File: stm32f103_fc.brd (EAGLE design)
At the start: 53.1 x 76.5 mm, 50 parts, among them IC1 STM32F103C8T6, IC2 LD1117AS33TR, Y1 8MHz, Y2 32.768MHz

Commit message: fix
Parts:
- flipped C22 to the top
- flipped R10 to the top, turned to 180 degrees
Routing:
- net GND: track 239.0 -> 236.5 mm
- net PA12: track 56.3 -> 58.3 mm
- net PA11: track 5.78 -> 4.51 mm, vias 1 -> 0
- net VCC3V3: track 252.3 -> 251.2 mm
- net N$16: track 5.27 -> 5.71 mm, vias 1 -> 2
- net N$6: track 66.7 -> 67.0 mm, vias 5 -> 6

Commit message: version 1.0.1 done fix transistor
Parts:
- removed N-CHANNEL-MOSFET: 2N7002KT1G, adafruit:SOT23
- removed R12: 1omh, SparkFun-Resistors:0603
- added MOSFET-1: 2N7002KT1G, adafruit:SOT23
- added R14: 470omh, SparkFun-Resistors:0603
- R4: value 470omh -> 1omh
- moved R4 40.3 mm to (58.2, 30.6)
- moved R15 25.6 mm to (58.8, 43.0), turned to 270 degrees
- moved R5 16.8 mm to (55.2, 70.4), turned to 180 degrees
- moved SERVO_X 1.02 mm to (68.3, 47.0)
- moved PY1 0.76 mm to (63.6, 28.7)
- renumbered N-CHANNEL-MOSFET-2 to MOSFET-2
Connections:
- removed net N$15: N-CHANNEL-MOSFET.3, R12.1
- new net N$11: PY1.2, R4.2
- net GND: now also MOSFET-1.3, MOSFET-2.3, R14.2, R5.2; no longer MOSFET-2.2, N-CHANNEL-MOSFET.2, R4.1, R5.1
- net N$13: now also MOSFET-2.2; no longer MOSFET-2.3
- net N$14: now also MOSFET-1.2, R4.1; no longer PY1.2, R12.2
- net PB6: now also R14.1; no longer R5.2
- net PB7: now also MOSFET-1.1, R5.1; no longer N-CHANNEL-MOSFET.1, R4.2
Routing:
- net N$12: track 39.7 -> 7.45 mm, vias 2 -> 1
- net GND: track 236.5 -> 207.1 mm, vias 12 -> 10
- net N$13: track 7.87 -> 28.6 mm, vias 0 -> 2
- net N$15: track 10.5 -> 0.00 mm, vias 2 -> 0
- net N$11: track 0.00 -> 5.70 mm
- net N$14: track 51.5 -> 55.7 mm
- net N$17: track 28.8 -> 30.7 mm
- net PB7: track 42.1 -> 43.8 mm
- net PB6: track 29.2 -> 30.7 mm
- net 9V: track 165.4 -> 166.2 mm
- net PA6: track 22.2 -> 22.8 mm

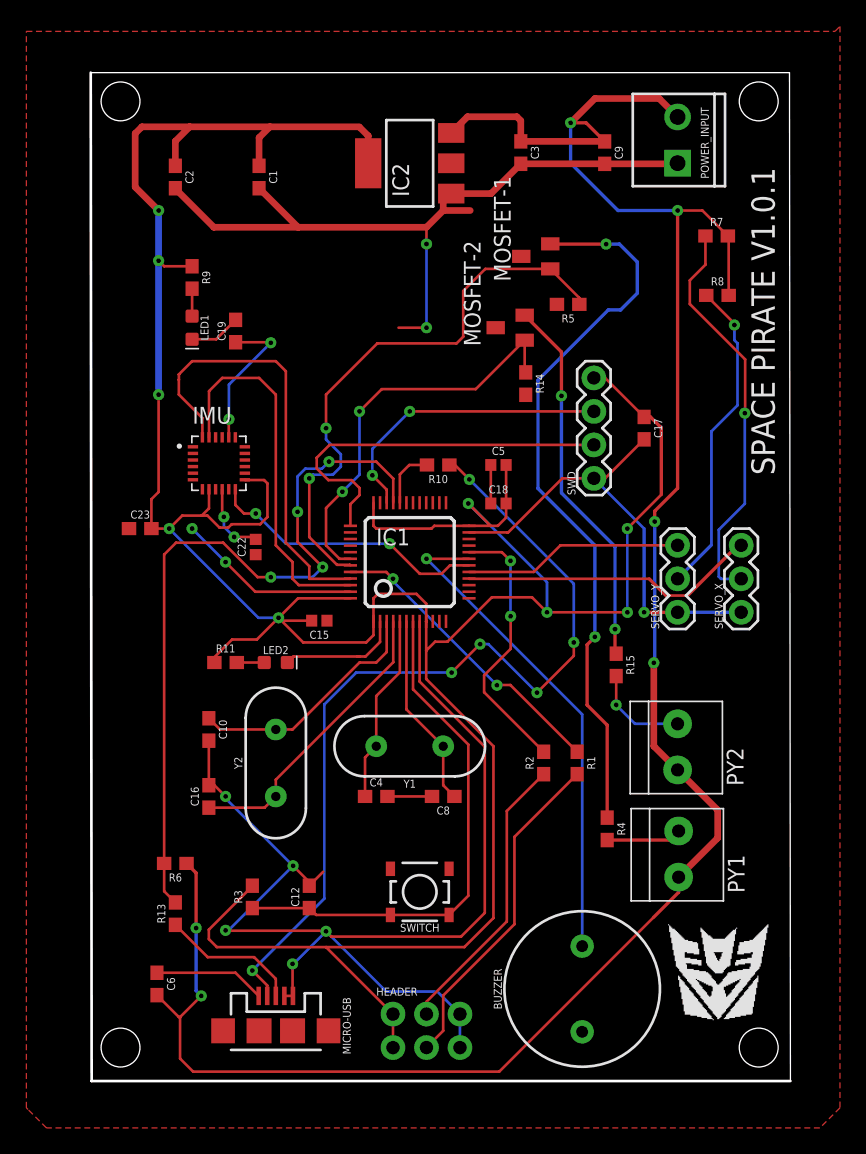
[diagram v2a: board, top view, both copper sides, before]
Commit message: four layer board done
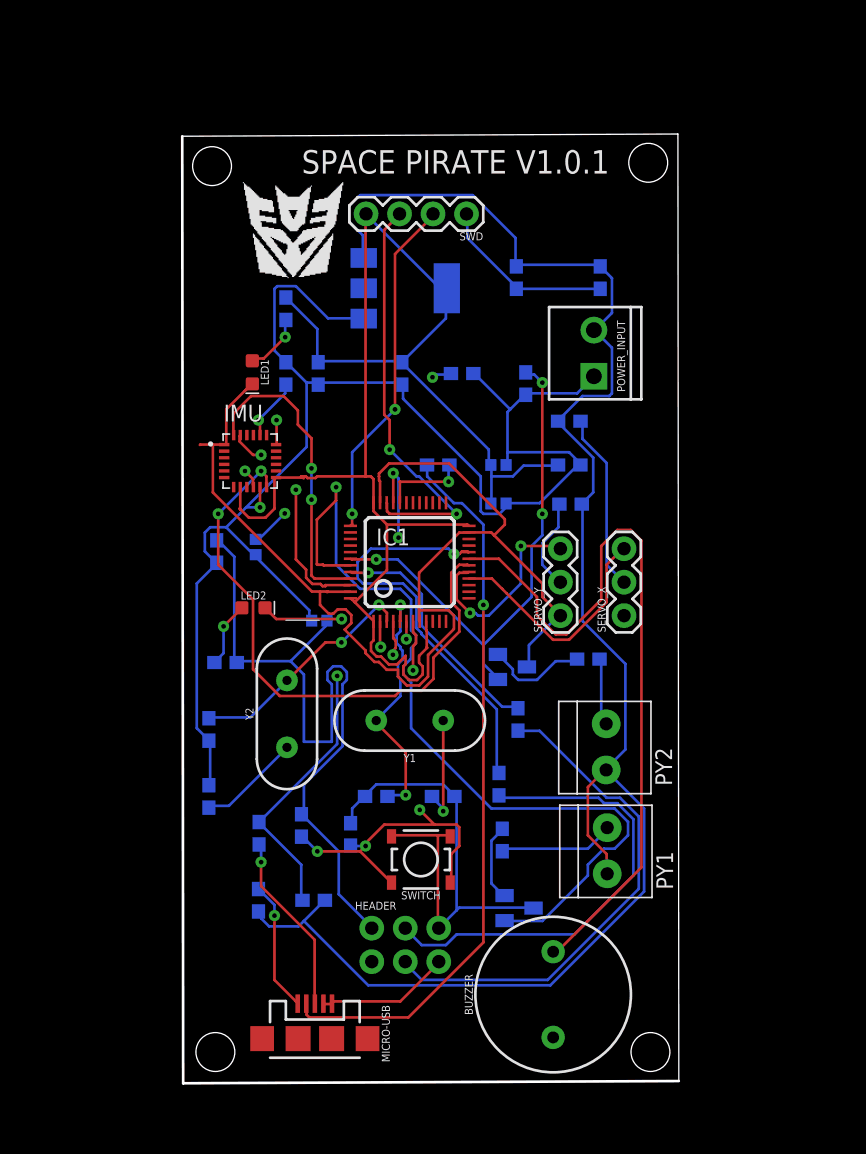
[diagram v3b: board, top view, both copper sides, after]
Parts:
- moved MOSFET-1 49.5 mm to (51.5, 24.6), flipped to the bottom
- moved MOSFET-2 25.7 mm to (51.0, 42.8), flipped to the bottom
- moved SWD 22.3 mm to (47.5, 77.2), turned to 180 degrees
- moved R8 19.4 mm to (55.4, 55.2), flipped to the bottom, turned to 180 degrees
- moved C1 18.4 mm to (42.6, 65.1), flipped to the bottom
- moved C2 18.4 mm to (36.2, 65.1), flipped to the bottom
- moved R7 18.0 mm to (55.3, 61.5), flipped to the bottom
- moved POWER_INPUT 17.4 mm to (57.2, 64.9)
- moved R6 10.9 mm to (35.9, 25.1), flipped to the bottom, turned to 0 degrees
- moved C6 9.98 mm to (31.7, 25.1), flipped to the bottom
- moved R5 9.60 mm to (47.2, 65.1), flipped to the bottom
- moved C3 9.49 mm to (51.3, 72.4), flipped to the bottom
- moved C9 9.49 mm to (57.6, 72.4), flipped to the bottom
- moved IC2 9.49 mm to (42.8, 71.6), flipped to the bottom
- moved SERVO_X 8.89 mm to (59.4, 46.7)
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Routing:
- net GND: track 207.1 -> 287.9 mm, vias 10 -> 2
- net VCC3V3: track 251.2 -> 172.4 mm, vias 9 -> 0
- net N$14: track 55.7 -> 5.84 mm, vias 2 -> 0
- net 9V: track 166.2 -> 130.1 mm, vias 6 -> 0
- net PB7: track 43.8 -> 78.1 mm
- net PB0: track 21.3 -> 44.6 mm
- net N$13: track 28.6 -> 7.69 mm, vias 2 -> 0
- net PB1: track 37.5 -> 56.5 mm, vias 1 -> 0
- net PA12: track 58.3 -> 40.6 mm, vias 4 -> 3
- net N$18: track 24.4 -> 7.03 mm, vias 1 -> 0
- net N$17: track 30.7 -> 13.6 mm, vias 1 -> 0
- net N$2: track 21.9 -> 35.3 mm
- net N$1: track 25.5 -> 38.6 mm
- net N$6: track 67.0 -> 55.0 mm, vias 6 -> 1
- net PB9: track 28.6 -> 17.0 mm, vias 0 -> 2
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- added copper zone on layer 15, net GND
- added copper zone on layer 2, net VCC3V3
- removed copper zone on layer 1, net GND
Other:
- board size 53.1 x 76.5 mm -> 37.7 x 72 mm

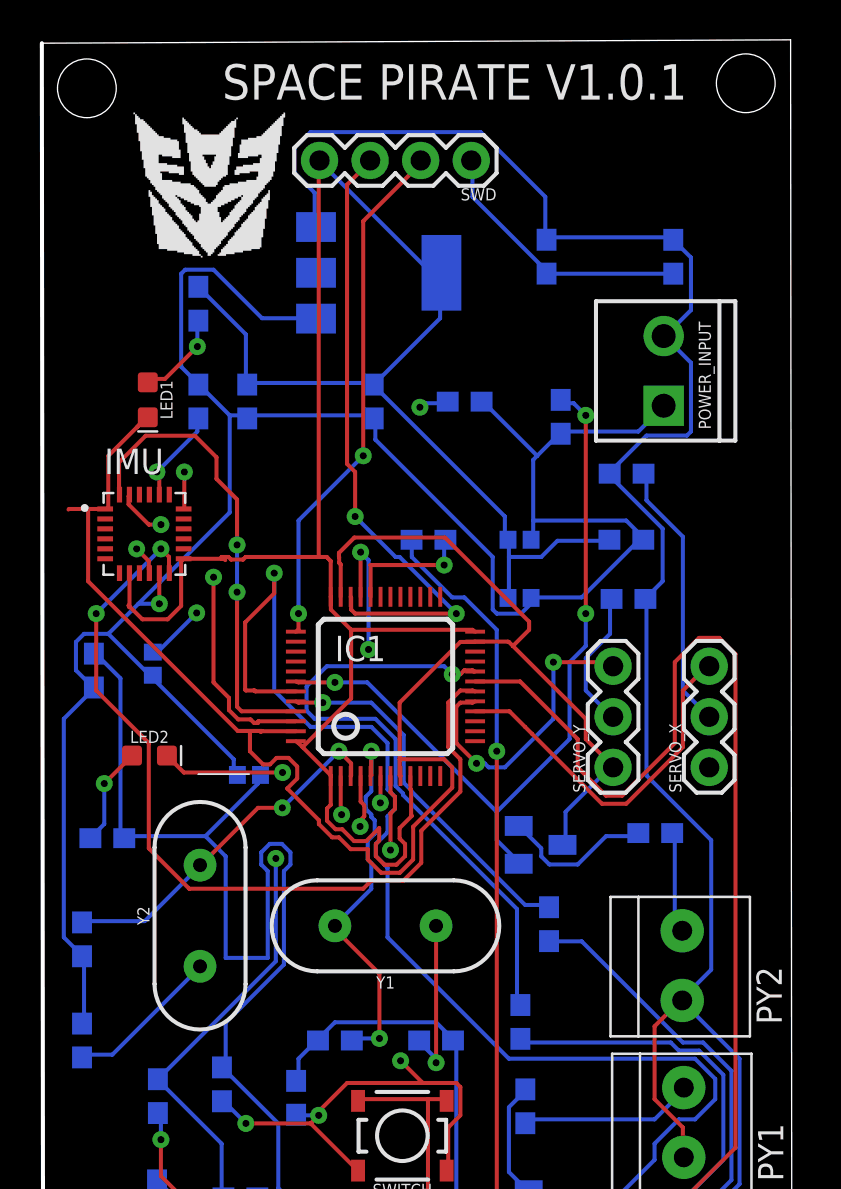
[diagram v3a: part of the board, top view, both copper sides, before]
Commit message: fixed mirror issue
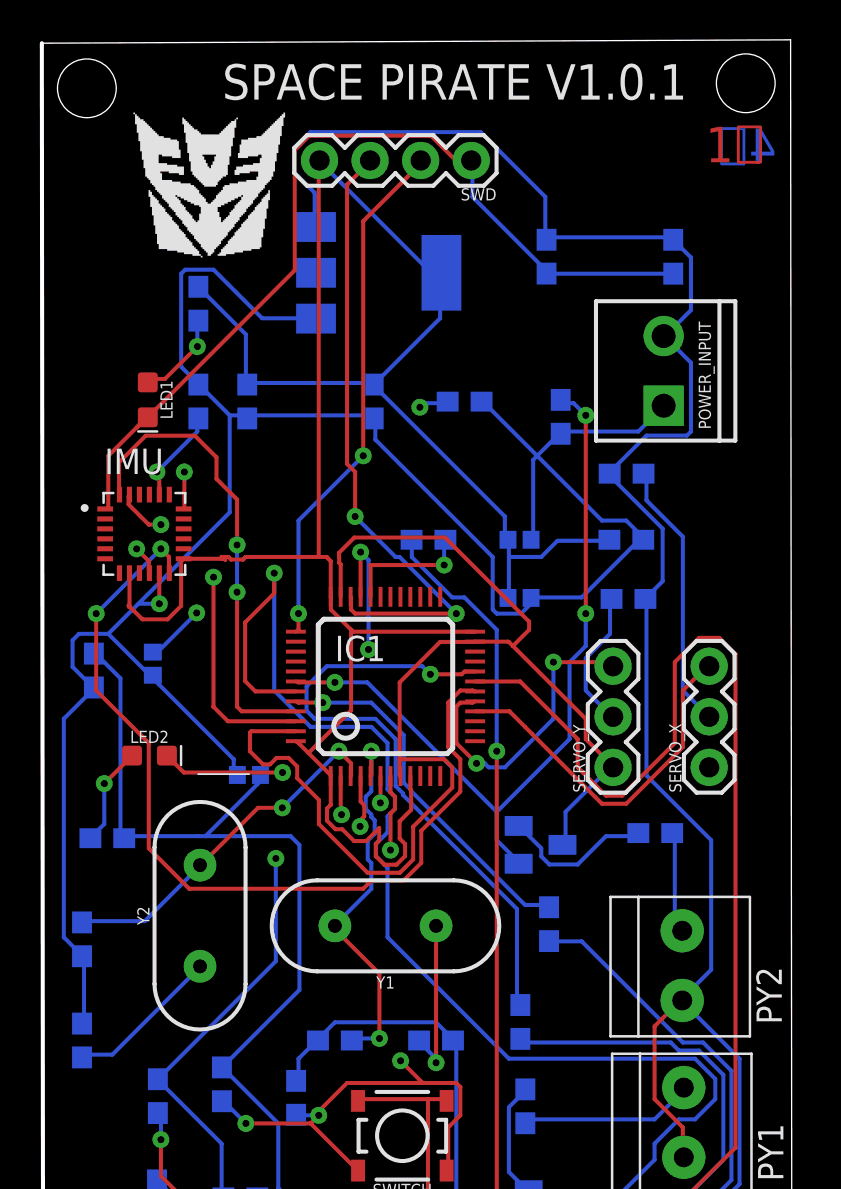
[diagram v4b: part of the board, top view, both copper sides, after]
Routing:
- net GND: track 287.9 -> 298.4 mm
- net VCC3V3: track 172.4 -> 162.2 mm
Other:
- board text added: "1层"
- board text added: "2层"
- board text added: "3层"
- board text added: "4层"

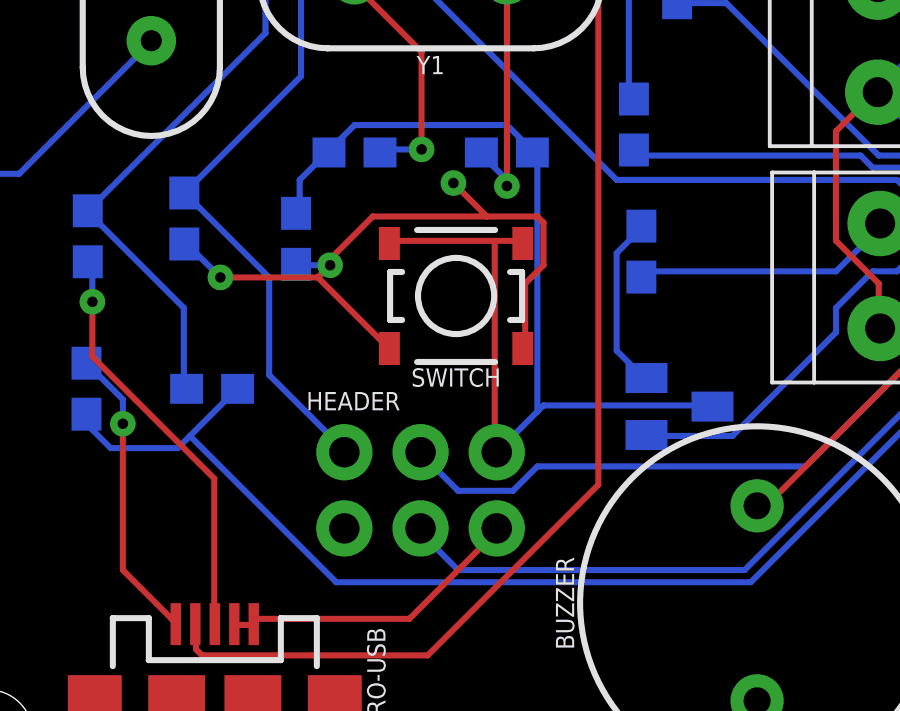
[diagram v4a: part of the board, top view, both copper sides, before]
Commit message: added new switch
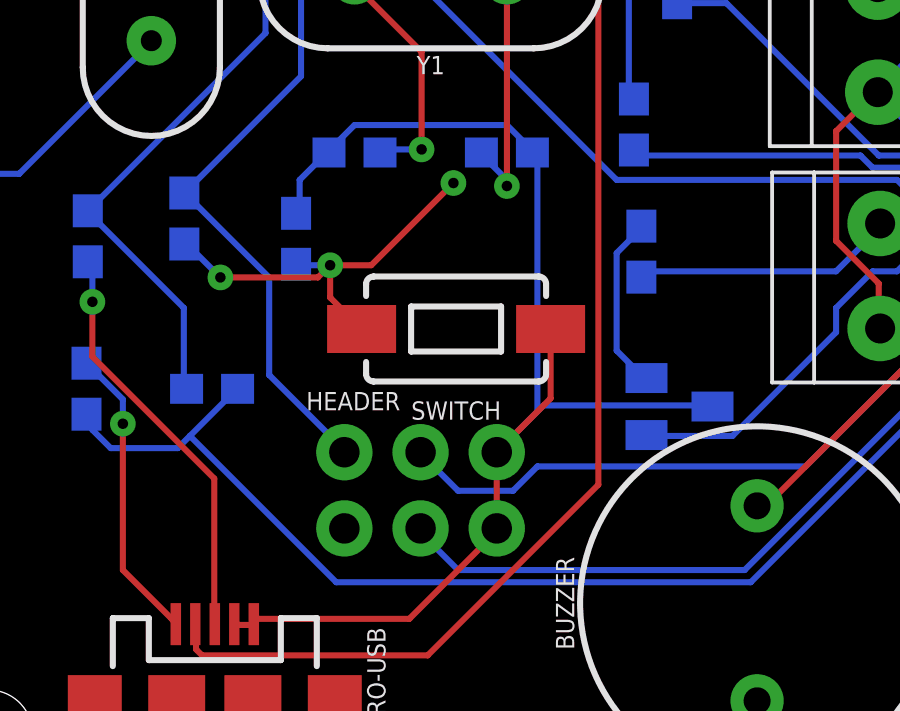
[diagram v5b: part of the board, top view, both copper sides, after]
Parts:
- SWITCH: device SparkFun-Switches:TACTILE_SWITCH_SMD_4.5MM -> SparkFun-Switches:TACTILE_SWITCH_SMD_6.0X3.5MM
- moved SWITCH 1.10 mm to (44.0, 27.1)
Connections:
- net GND: now also SWITCH.1; no longer SWITCH.2, SWITCH.3
- net RESET: now also SWITCH.2; no longer SWITCH.1, SWITCH.4
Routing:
- net RESET: track 38.7 -> 29.1 mm
- net GND: track 298.4 -> 294.2 mm
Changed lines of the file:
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@@
 <?xml version="1.0" encoding="utf-8"?>
 <!DOCTYPE eagle SYSTEM "eagle.dtd">
-<eagle version="9.3.1">
+<eagle version="9.3.0">
 <drawing>
 <settings>
@@
 <attribute name="VALUE" x="49.911" y="54.483" size="0.6096" layer="28" font="vector" ratio="20" rot="MR0" align="top-center"/>
 </element>
-<element name="SWITCH" library="SparkFun-Switches" library_urn="urn:adsk.eagle:library:535" package="TACTILE_SWITCH_SMD_4.5MM" package3d_urn="urn:adsk.eagle:package:40162/1" value="MOMENTARY-SWITCH-SPST-SMD-4.5MM-轻触开关" x="44.026659375" y="28.2360875" smashed="yes" rot="R180">
-<attribute name="NAME" x="44.026659375" y="25.8230875" size="0.6096" layer="21" font="vector" ratio="20" rot="R180" align="bottom-center"/>
-<attribute name="PROD_ID" value="SWCH-09213" x="44.026659375" y="28.2360875" size="1.778" layer="27" rot="R180" display="off"/>
-<attribute name="VALUE" x="44.026659375" y="30.6490875" size="0.6096" layer="27" font="vector" ratio="20" rot="R180" align="top-center"/>
+<element name="SWITCH" library="SparkFun-Switches" library_urn="urn:adsk.eagle:library:535" package="TACTILE_SWITCH_SMD_6.0X3.5MM" package3d_urn="urn:adsk.eagle:package:40165/1" value="MOMENTARY-SWITCH-SPST-SMD-4.5MM-轻触开关" x="44.0266625" y="27.13553125" smashed="yes" rot="R180">
+<attribute name="NAME" x="44.0266625" y="24.72253125" size="0.6096" layer="21" font="vector" ratio="20" rot="R180" align="bottom-center"/>
+<attribute name="PROD_ID" value="SWCH-00815" x="44.0266625" y="27.13553125" size="1.778" layer="27" rot="R180" display="off"/>
+<attribute name="SF_SKU" value="COM-08229" x="44.0266625" y="27.13553125" size="1.778" layer="27" rot="R180" display="off"/>
+<attribute name="VALUE" x="44.0266625" y="29.54853125" size="0.6096" layer="27" font="vector" ratio="20" rot="R180" align="top-center"/>
 </element>
 <element name="R14" library="SparkFun-Resistors" library_urn="urn:adsk.eagle:library:532" package="0603" package3d_urn="urn:adsk.eagle:package:39650/1" value="470omh" x="51.980140625" y="64.340234375" smashed="yes" rot="MR270">
@@
 <contactref element="IC1" pad="35"/>
 <contactref element="IC1" pad="8"/>
-<contactref element="SWITCH" pad="2"/>
-<contactref element="SWITCH" pad="3"/>
+<contactref element="SWITCH" pad="1"/>
 <contactref element="R14" pad="2"/>
 <contactref element="MOSFET-2" pad="3"/>
@@
 <wire x1="57.5056" y1="71.5264" x2="57.632025" y2="71.529334375" width="0.2032" layer="16"/>
 <wire x1="51.4096" y1="71.5264" x2="51.268534375" y2="71.53258125" width="0.2032" layer="16"/>
-<wire x1="46.1264" y1="30.0736" x2="45.3136" y2="30.0736" width="0.2032" layer="1"/>
-<wire x1="45.3136" y1="30.0736" x2="41.8592" y2="30.0736" width="0.2032" layer="1"/>
-<wire x1="41.8592" y1="30.0736" x2="41.801659375" y2="29.9860875" width="0.2032" layer="1"/>
-<wire x1="46.1264" y1="30.0736" x2="46.251659375" y2="29.9860875" width="0.2032" layer="1"/>
 <wire x1="37.1856" y1="17.272" x2="36.7792" y2="17.272" width="0.2032" layer="1"/>
 <wire x1="36.7792" y1="17.272" x2="36.6330375" y2="17.297390625" width="0.2032" layer="1"/>
@@
 <wire x1="37.3888" y1="17.4752" x2="37.2830375" y2="17.297390625" width="0.2032" layer="1"/>
 <wire x1="45.3136" y1="20.32" x2="45.381490625" y2="20.48868125" width="0.2032" layer="1"/>
-<wire x1="45.3136" y1="23.1648" x2="45.3136" y2="30.0736" width="0.2032" layer="1"/>
-<wire x1="45.381490625" y1="23.02868125" x2="45.3136" y2="23.1648" width="0.2032" layer="1"/>
 <wire x1="47.5488" y1="75.3872" x2="51.2064" y2="71.7296" width="0.2032" layer="16"/>
 <wire x1="47.5488" y1="77.0128" x2="47.5488" y2="75.3872" width="0.2032" layer="16"/>
@@
 <wire x1="38.622928125" y1="71.698059375" x2="38.622928125" y2="77.729521875" width="0.2032" layer="1"/>
 <wire x1="39.352003125" y1="78.458596875" x2="45.463065625" y2="78.458596875" width="0.2032" layer="1"/>
+<wire x1="47.1766625" y1="27.13553125" x2="47.1766625" y2="24.823853125" width="0.2032" layer="1"/>
+<wire x1="47.1766625" y1="24.823853125" x2="45.381490625" y2="23.02868125" width="0.2032" layer="1"/>
+<wire x1="45.381490625" y1="20.48868125" x2="45.381490625" y2="23.02868125" width="0.2032" layer="1"/>
 </signal>
 <signal name="N$3">
@@
 <contactref element="C12" pad="1"/>
 <contactref element="R3" pad="1"/>
-<contactref element="SWITCH" pad="4"/>
-<contactref element="SWITCH" pad="1"/>
+<contactref element="SWITCH" pad="2"/>
 <wire x1="36.1696" y1="28.8544" x2="35.1536" y2="29.8704" width="0.2032" layer="16"/>
 <wire x1="39.4208" y1="28.8544" x2="36.1696" y2="28.8544" width="0.2032" layer="1"/>
-<wire x1="41.656" y1="26.6192" x2="39.4208" y2="28.8544" width="0.2032" layer="1"/>
 <wire x1="35.1536" y1="29.8704" x2="34.966959375" y2="29.968125" width="0.2032" layer="16"/>
-<wire x1="41.656" y1="26.6192" x2="41.801659375" y2="26.4860875" width="0.2032" layer="1"/>
 <wire x1="39.8272" y1="29.2608" x2="38.8112" y2="29.2608" width="0.2032" layer="16"/>
 <wire x1="39.4208" y1="28.8544" x2="39.8272" y2="29.2608" width="0.2032" layer="1"/>
 <wire x1="38.8112" y1="29.2608" x2="38.692353125" y2="29.290859375" width="0.2032" layer="16"/>
-<wire x1="46.3296" y1="28.6512" x2="46.3296" y2="26.6192" width="0.2032" layer="1"/>
-<wire x1="46.9392" y1="29.2608" x2="46.3296" y2="28.6512" width="0.2032" layer="1"/>
-<wire x1="46.9392" y1="30.6832" x2="46.9392" y2="29.2608" width="0.2032" layer="1"/>
-<wire x1="46.736" y1="30.8864" x2="46.9392" y2="30.6832" width="0.2032" layer="1"/>
-<wire x1="41.2496" y1="30.8864" x2="45.05200625" y2="30.8864" width="0.2032" layer="1"/>
-<wire x1="45.05200625" y1="30.8864" x2="46.736" y2="30.8864" width="0.2032" layer="1"/>
-<wire x1="39.8272" y1="29.464" x2="41.2496" y2="30.8864" width="0.2032" layer="1"/>
-<wire x1="39.8272" y1="29.2608" x2="39.8272" y2="29.464" width="0.2032" layer="1"/>
-<wire x1="46.3296" y1="26.6192" x2="46.251659375" y2="26.4860875" width="0.2032" layer="1"/>
 <via x="36.1696" y="28.8544" extent="1-16" drill="0.35"/>
 <via x="39.8272" y="29.2608" extent="1-16" drill="0.35"/>
@@
 <wire x1="43.609" y1="32.32940625" x2="43.93760625" y2="32.0008" width="0.2032" layer="2"/>
 <wire x1="43.609" y1="33.42555" x2="43.609" y2="32.32940625" width="0.2032" layer="2"/>
-<wire x1="43.93760625" y1="32.0008" x2="45.05200625" y2="30.8864" width="0.2032" layer="1"/>
 <wire x1="43.43" y1="46.3" x2="43.43" y2="45.48296875" width="0.2032" layer="1"/>
 <wire x1="43.43" y1="45.48296875" x2="43.6555125" y2="45.25745625" width="0.2032" layer="1"/>
@@
 <wire x1="43.42965625" y1="44.4237" x2="43.6555125" y2="44.64955625" width="0.2032" layer="1"/>
 <wire x1="43.42965625" y1="42.583075" x2="43.42965625" y2="44.4237" width="0.2032" layer="1"/>
+<wire x1="40.8766625" y1="27.13553125" x2="39.8272" y2="28.18499375" width="0.2032" layer="1"/>
+<wire x1="39.8272" y1="28.18499375" x2="39.8272" y2="29.2608" width="0.2032" layer="1"/>
+<wire x1="43.93760625" y1="32.0008" x2="41.19760625" y2="29.2608" width="0.2032" layer="1"/>
+<wire x1="41.19760625" y1="29.2608" x2="39.8272" y2="29.2608" width="0.2032" layer="1"/>
 </signal>
 <signal name="N$6">
